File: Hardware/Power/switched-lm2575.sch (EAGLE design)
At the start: 8 parts

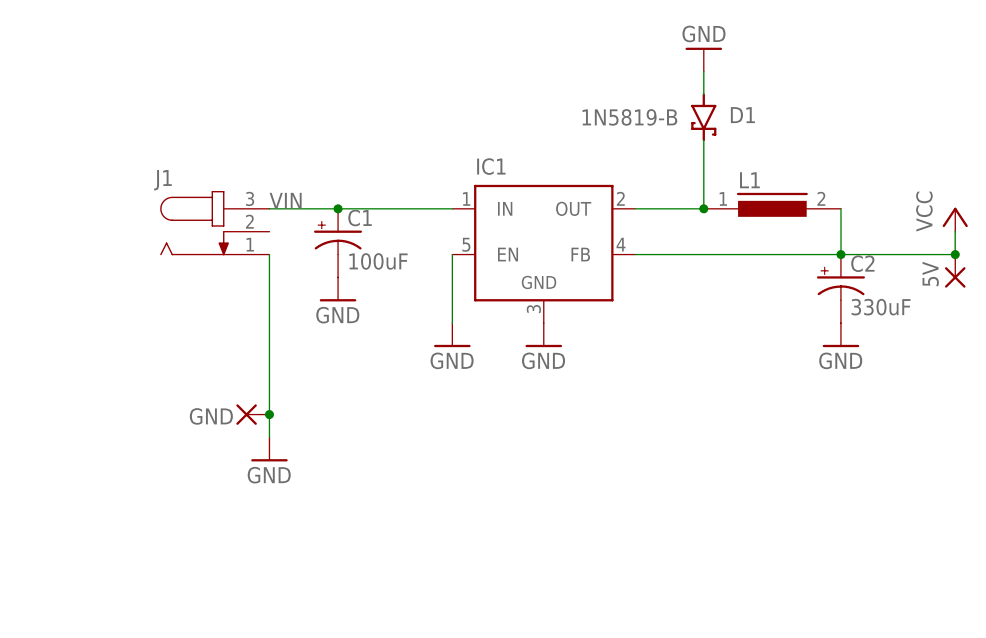
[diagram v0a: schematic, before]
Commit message: Updates to combined board inc. new blitter features
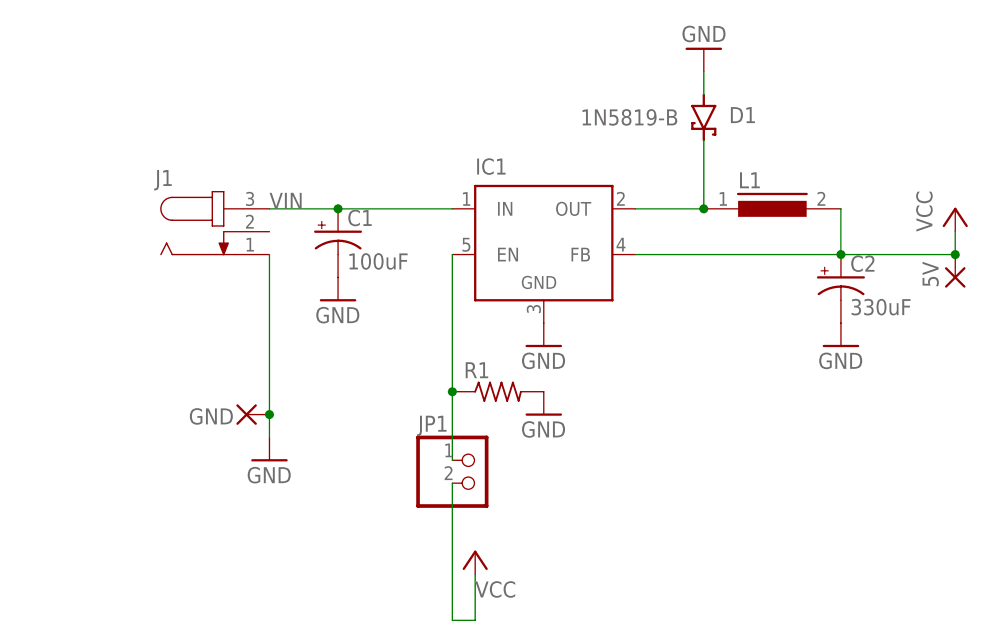
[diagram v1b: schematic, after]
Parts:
- added JP1: (no value), pinhead:PINHD-1X2
- added R1: (no value), rcl:R-US_0207/10
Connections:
- new net N$3: IC1.EN, JP1.1, R1.1
- net GND: now also R1.2; no longer IC1.EN
- net VCC: now also JP1.2
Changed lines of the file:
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@@
 <part name="GND3" library="supply1" library_urn="urn:adsk.eagle:library:371" deviceset="GND" device=""/>
 <part name="GND4" library="supply1" library_urn="urn:adsk.eagle:library:371" deviceset="GND" device=""/>
+<part name="GND6" library="supply1" library_urn="urn:adsk.eagle:library:371" deviceset="GND" device=""/>
+<part name="JP1" library="pinhead" library_urn="urn:adsk.eagle:library:325" deviceset="PINHD-1X2" device="" package3d_urn="urn:adsk.eagle:package:22435/2"/>
+<part name="R1" library="rcl" library_urn="urn:adsk.eagle:library:334" deviceset="R-US_" device="0207/10" package3d_urn="urn:adsk.eagle:package:23491/2"/>
 <part name="GND5" library="supply1" library_urn="urn:adsk.eagle:library:371" deviceset="GND" device=""/>
-<part name="GND6" library="supply1" library_urn="urn:adsk.eagle:library:371" deviceset="GND" device=""/>
+<part name="P+2" library="supply1" library_urn="urn:adsk.eagle:library:371" deviceset="VCC" device=""/>
 </parts>
 <sheets>
@@
 <attribute name="VALUE" x="12.7" y="71.12" size="1.778" layer="96"/>
 </instance>
-<instance part="GND5" gate="1" x="27.94" y="68.58" smashed="yes">
-<attribute name="VALUE" x="25.4" y="66.04" size="1.778" layer="96"/>
-</instance>
 <instance part="GND6" gate="1" x="71.12" y="68.58" smashed="yes">
 <attribute name="VALUE" x="68.58" y="66.04" size="1.778" layer="96"/>
+</instance>
+<instance part="JP1" gate="G$1" x="30.48" y="53.34" smashed="yes">
+<attribute name="NAME" x="24.13" y="59.055" size="1.778" layer="95"/>
+<attribute name="VALUE" x="24.13" y="48.26" size="1.778" layer="96"/>
+</instance>
+<instance part="R1" gate="G$1" x="33.02" y="63.5" smashed="yes">
+<attribute name="NAME" x="29.21" y="64.9986" size="1.778" layer="95"/>
+<attribute name="VALUE" x="29.21" y="60.198" size="1.778" layer="96"/>
+</instance>
+<instance part="GND5" gate="1" x="38.1" y="60.96" smashed="yes">
+<attribute name="VALUE" x="35.56" y="58.42" size="1.778" layer="96"/>
+</instance>
+<instance part="P+2" gate="VCC" x="30.48" y="45.72" smashed="yes">
+<attribute name="VALUE" x="30.48" y="40.64" size="1.778" layer="96"/>
 </instance>
 </instances>
@@
 <pinref part="L1" gate="1" pin="2"/>
 <wire x1="71.12" y1="78.74" x2="71.12" y2="83.82" width="0.1524" layer="91"/>
+</segment>
+<segment>
+<pinref part="JP1" gate="G$1" pin="2"/>
+<wire x1="27.94" y1="53.34" x2="27.94" y2="38.1" width="0.1524" layer="91"/>
+<wire x1="27.94" y1="38.1" x2="30.48" y2="38.1" width="0.1524" layer="91"/>
+<pinref part="P+2" gate="VCC" pin="VCC"/>
+<wire x1="30.48" y1="38.1" x2="30.48" y2="43.18" width="0.1524" layer="91"/>
 </segment>
 </net>
@@
 </segment>
 <segment>
-<pinref part="IC1" gate="NC1" pin="EN"/>
-<pinref part="GND5" gate="1" pin="GND"/>
-<wire x1="27.94" y1="78.74" x2="27.94" y2="71.12" width="0.1524" layer="91"/>
+<pinref part="C2" gate="G$1" pin="-"/>
+<pinref part="GND6" gate="1" pin="GND"/>
 </segment>
 <segment>
-<pinref part="C2" gate="G$1" pin="-"/>
-<pinref part="GND6" gate="1" pin="GND"/>
+<pinref part="R1" gate="G$1" pin="2"/>
+<pinref part="GND5" gate="1" pin="GND"/>
 </segment>
 </net>
@@
 </segment>
 </net>
+<net name="N$3" class="0">
+<segment>
+<pinref part="JP1" gate="G$1" pin="1"/>
+<pinref part="R1" gate="G$1" pin="1"/>
+<wire x1="27.94" y1="55.88" x2="27.94" y2="63.5" width="0.1524" layer="91"/>
+<pinref part="IC1" gate="NC1" pin="EN"/>
+<wire x1="27.94" y1="63.5" x2="27.94" y2="78.74" width="0.1524" layer="91"/>
+<junction x="27.94" y="63.5"/>
+</segment>
+</net>

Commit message: RTC flash and power supply update
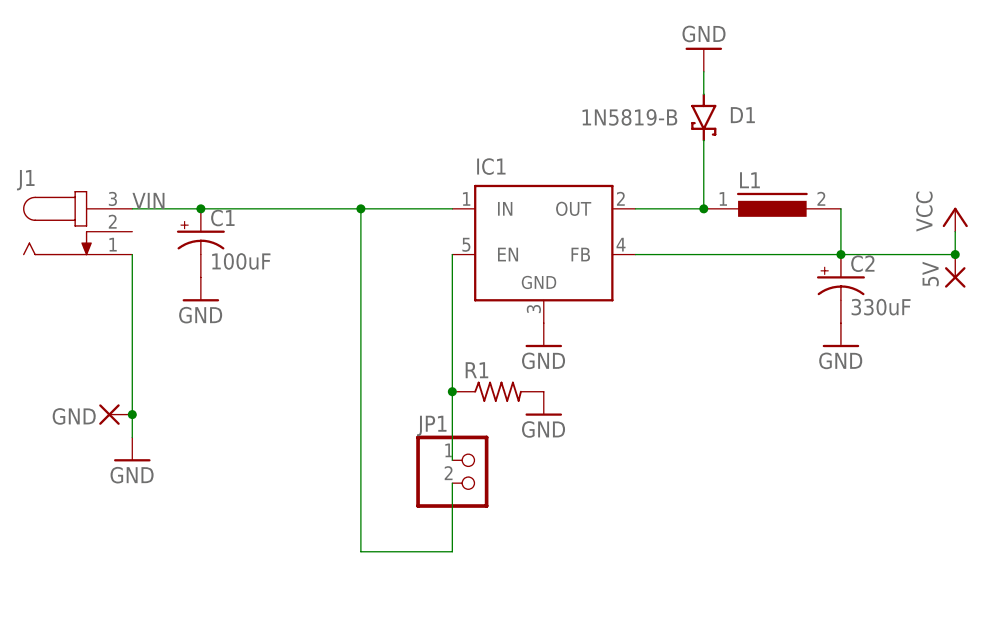
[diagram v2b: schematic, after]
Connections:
- net VCC: no longer JP1.2
- net VIN: now also JP1.2
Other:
- moved on the sheet: C1, GND, J1
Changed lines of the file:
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@@
 <part name="R1" library="rcl" library_urn="urn:adsk.eagle:library:334" deviceset="R-US_" device="0207/10" package3d_urn="urn:adsk.eagle:package:23491/2"/>
 <part name="GND5" library="supply1" library_urn="urn:adsk.eagle:library:371" deviceset="GND" device=""/>
-<part name="P+2" library="supply1" library_urn="urn:adsk.eagle:library:371" deviceset="VCC" device=""/>
 </parts>
 <sheets>
@@
 </plain>
 <instances>
-<instance part="GND" gate="1" x="5.08" y="60.96" smashed="yes">
-<attribute name="NAME" x="3.683" y="61.6458" size="1.778" layer="95" rot="R180"/>
-<attribute name="VALUE" x="3.937" y="57.658" size="1.778" layer="96"/>
+<instance part="GND" gate="1" x="-10.16" y="60.96" smashed="yes">
+<attribute name="NAME" x="-11.557" y="61.6458" size="1.778" layer="95" rot="R180"/>
+<attribute name="VALUE" x="-11.303" y="57.658" size="1.778" layer="96"/>
 </instance>
 <instance part="5V" gate="1" x="83.82" y="76.2" smashed="yes" rot="R90">
@@
 <attribute name="VALUE" x="40.64" y="87.63" size="1.778" layer="96"/>
 </instance>
-<instance part="GND1" gate="1" x="7.62" y="55.88" smashed="yes">
-<attribute name="VALUE" x="5.08" y="53.34" size="1.778" layer="96"/>
+<instance part="GND1" gate="1" x="-7.62" y="55.88" smashed="yes">
+<attribute name="VALUE" x="-10.16" y="53.34" size="1.778" layer="96"/>
 </instance>
 <instance part="P+1" gate="VCC" x="83.82" y="83.82" smashed="yes">
 <attribute name="VALUE" x="81.28" y="81.28" size="1.778" layer="96" rot="R90"/>
 </instance>
-<instance part="J1" gate="G$1" x="2.54" y="81.28" smashed="yes">
-<attribute name="NAME" x="-5.08" y="86.36" size="1.778" layer="95"/>
-<attribute name="VALUE" x="-5.08" y="76.2" size="1.778" layer="96"/>
+<instance part="J1" gate="G$1" x="-12.7" y="81.28" smashed="yes">
+<attribute name="NAME" x="-20.32" y="86.36" size="1.778" layer="95"/>
+<attribute name="VALUE" x="-20.32" y="76.2" size="1.778" layer="96"/>
 </instance>
-<instance part="C1" gate="G$1" x="15.24" y="81.28" smashed="yes">
-<attribute name="NAME" x="16.256" y="81.915" size="1.778" layer="95"/>
-<attribute name="VALUE" x="16.256" y="77.089" size="1.778" layer="96"/>
+<instance part="C1" gate="G$1" x="0" y="81.28" smashed="yes">
+<attribute name="NAME" x="1.016" y="81.915" size="1.778" layer="95"/>
+<attribute name="VALUE" x="1.016" y="77.089" size="1.778" layer="96"/>
 </instance>
 <instance part="C2" gate="G$1" x="71.12" y="76.2" smashed="yes">
@@
 <attribute name="VALUE" x="35.56" y="66.04" size="1.778" layer="96"/>
 </instance>
-<instance part="GND4" gate="1" x="15.24" y="73.66" smashed="yes">
-<attribute name="VALUE" x="12.7" y="71.12" size="1.778" layer="96"/>
+<instance part="GND4" gate="1" x="0" y="73.66" smashed="yes">
+<attribute name="VALUE" x="-2.54" y="71.12" size="1.778" layer="96"/>
 </instance>
 <instance part="GND6" gate="1" x="71.12" y="68.58" smashed="yes">
@@
 <instance part="GND5" gate="1" x="38.1" y="60.96" smashed="yes">
 <attribute name="VALUE" x="35.56" y="58.42" size="1.778" layer="96"/>
-</instance>
-<instance part="P+2" gate="VCC" x="30.48" y="45.72" smashed="yes">
-<attribute name="VALUE" x="30.48" y="40.64" size="1.778" layer="96"/>
 </instance>
 </instances>
@@
 <wire x1="71.12" y1="78.74" x2="71.12" y2="83.82" width="0.1524" layer="91"/>
 </segment>
-<segment>
-<pinref part="JP1" gate="G$1" pin="2"/>
-<wire x1="27.94" y1="53.34" x2="27.94" y2="38.1" width="0.1524" layer="91"/>
-<wire x1="27.94" y1="38.1" x2="30.48" y2="38.1" width="0.1524" layer="91"/>
-<pinref part="P+2" gate="VCC" pin="VCC"/>
-<wire x1="30.48" y1="38.1" x2="30.48" y2="43.18" width="0.1524" layer="91"/>
-</segment>
 </net>
 <net name="GND" class="0">
@@
 <pinref part="GND" gate="1" pin="P"/>
 <pinref part="GND1" gate="1" pin="GND"/>
-<wire x1="7.62" y1="60.96" x2="7.62" y2="58.42" width="0.1524" layer="91"/>
+<wire x1="-7.62" y1="60.96" x2="-7.62" y2="58.42" width="0.1524" layer="91"/>
 <pinref part="J1" gate="G$1" pin="1"/>
-<wire x1="7.62" y1="78.74" x2="7.62" y2="60.96" width="0.1524" layer="91"/>
-<junction x="7.62" y="60.96"/>
+<wire x1="-7.62" y1="78.74" x2="-7.62" y2="60.96" width="0.1524" layer="91"/>
+<junction x="-7.62" y="60.96"/>
 </segment>
 <segment>
@@
 <pinref part="J1" gate="G$1" pin="3"/>
 <pinref part="IC1" gate="NC1" pin="IN"/>
-<wire x1="7.62" y1="83.82" x2="15.24" y2="83.82" width="0.1524" layer="91"/>
+<wire x1="-7.62" y1="83.82" x2="0" y2="83.82" width="0.1524" layer="91"/>
 <pinref part="C1" gate="G$1" pin="+"/>
-<wire x1="15.24" y1="83.82" x2="27.94" y2="83.82" width="0.1524" layer="91"/>
-<junction x="15.24" y="83.82"/>
-<label x="7.62" y="83.82" size="1.778" layer="95"/>
+<wire x1="0" y1="83.82" x2="17.78" y2="83.82" width="0.1524" layer="91"/>
+<junction x="0" y="83.82"/>
+<label x="-7.62" y="83.82" size="1.778" layer="95"/>
+<wire x1="17.78" y1="83.82" x2="27.94" y2="83.82" width="0.1524" layer="91"/>
+<wire x1="17.78" y1="45.72" x2="17.78" y2="83.82" width="0.1524" layer="91"/>
+<junction x="17.78" y="83.82"/>
+<pinref part="JP1" gate="G$1" pin="2"/>
+<wire x1="27.94" y1="45.72" x2="27.94" y2="53.34" width="0.1524" layer="91"/>
+<wire x1="17.78" y1="45.72" x2="27.94" y2="45.72" width="0.1524" layer="91"/>
 </segment>
 </net>
